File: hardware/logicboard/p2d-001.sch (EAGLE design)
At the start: 54 parts, among them IC1 74LS06N, IC2 4066N, J1 MKR, J2 GPIO, J3 Vcc, J4 RLY, J5 SPI, K1 G5V1, T1 2SC1815, U1 DS18B20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

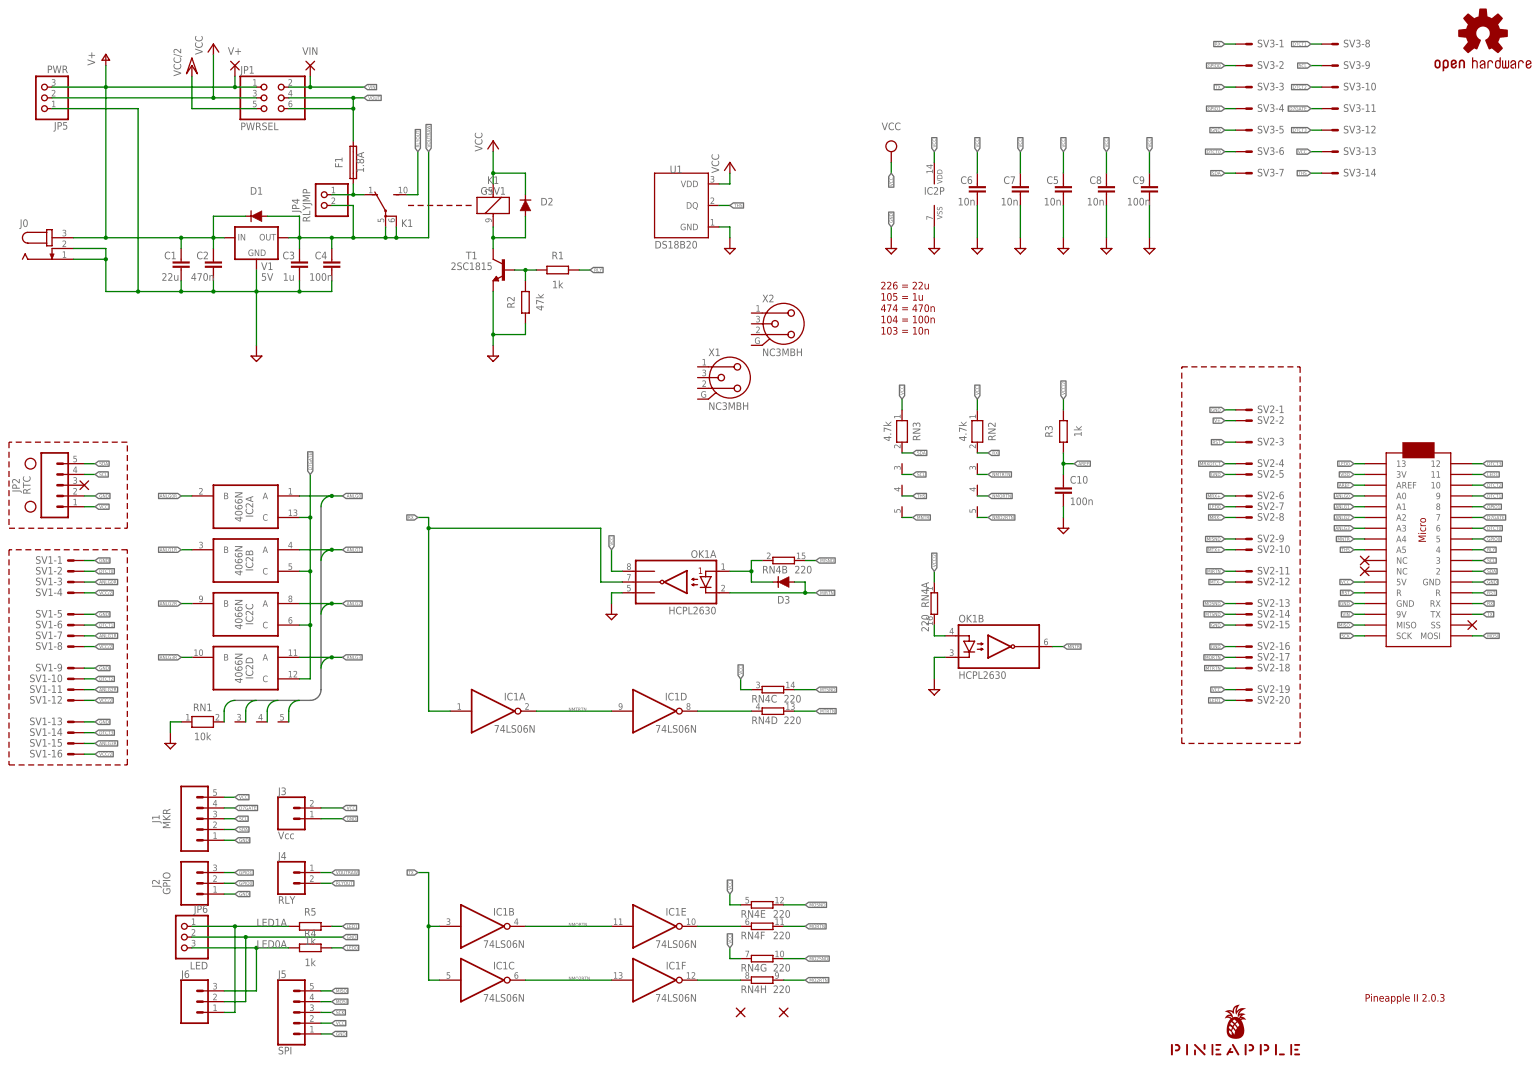
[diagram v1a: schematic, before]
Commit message: Put all parts on board.
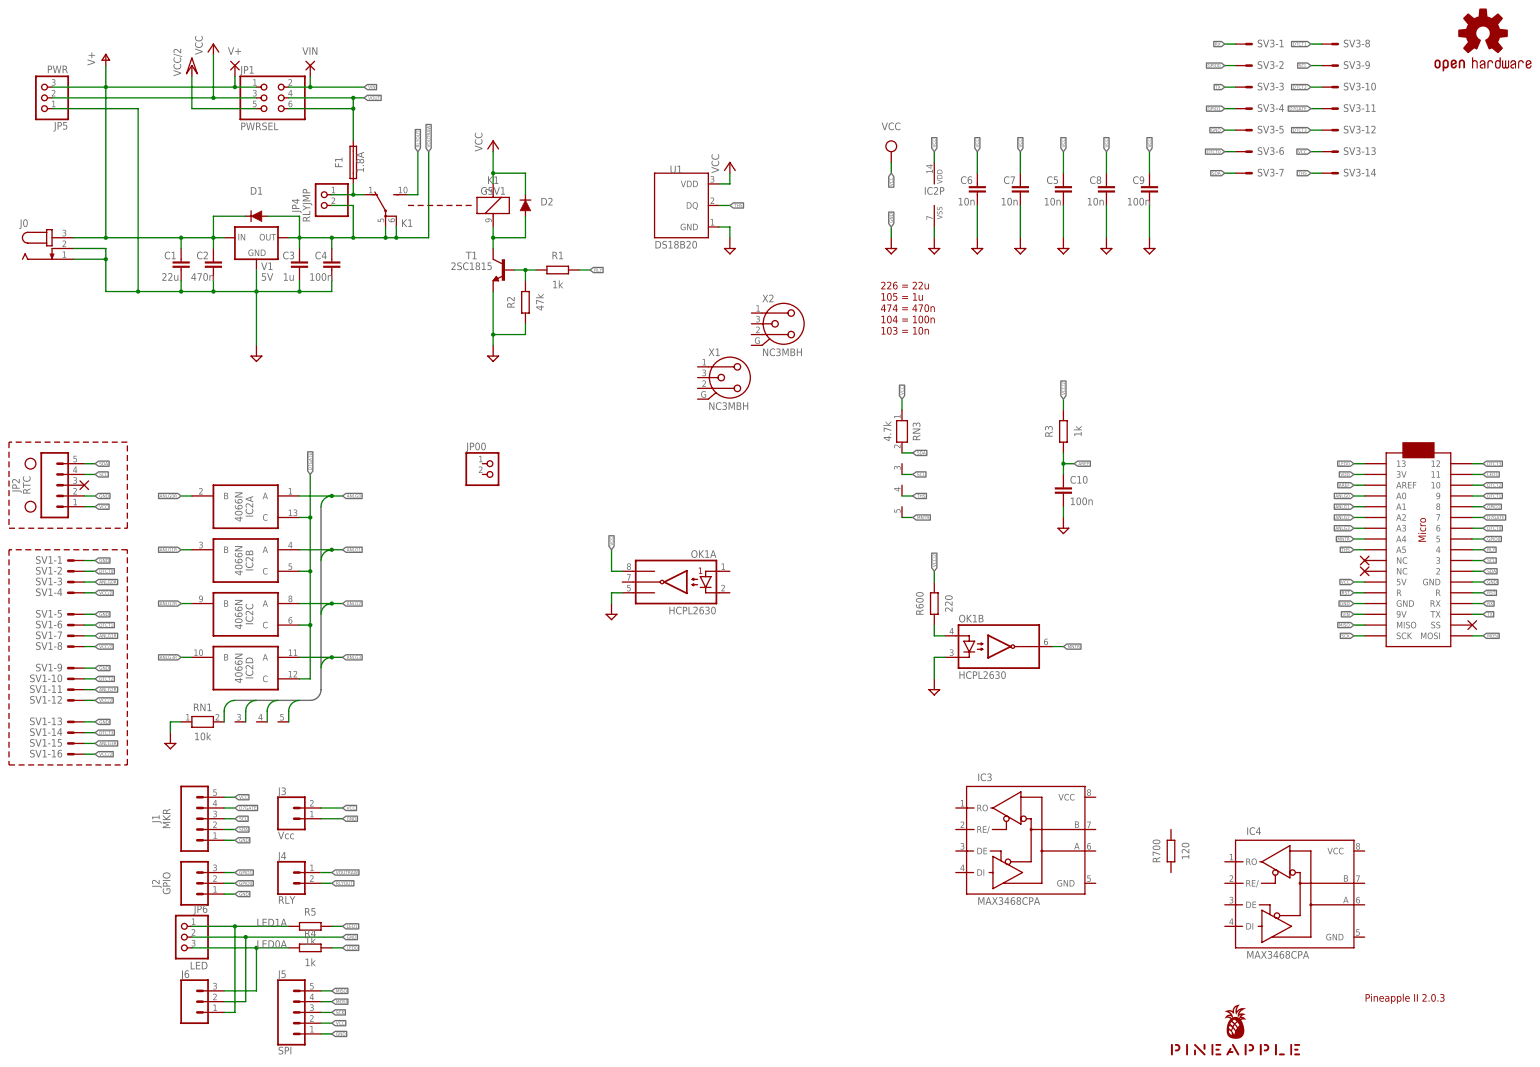
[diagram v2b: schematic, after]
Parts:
- removed D3: DIODE-1N4148, SparkFun-DiscreteSemi:DIODE-1N4148
- removed IC1: 74LS06N, 74xx-us:74LS06N
- removed RN2: 4.7k, resistor-net:RN04
- removed RN4: 220, resistor-dil:8R-N
- removed SV2: (no value), con-ml:ML20LE
- added IC3, IC4: MAX3468CPA, maxim:MAX3468CPA
- added JP00: (no value), pinhead:PINHD-1X2
- added R600: 220, resistor:R-EU_0204/5
- added R700: 120, resistor:R-EU_0204/5
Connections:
- removed net MIDIINSND: D3.C, OK1A.A1, RN4B.1
- removed net MIRTN: D3.A, OK1A.C1, SV2-11.S
- removed net MISND: RN4B.2, SV2-9.S
- removed net MO2RTN: RN4H.2
- removed net MO2RTNRAW: IC1F.O, RN4H.1
- removed net MO2SND: RN4G.2
- removed net MORTN: RN4F.2, SV2-17.S
- removed net MORTNRAW: IC1E.O, RN4F.1
- removed net MOSND: RN4E.2, SV2-13.S
- removed net MRX+: SV2-6.S
- removed net MRX-: SV2-8.S
- removed net MRXDTCT: SV2-4.S
- removed net MTRTN: RN4D.2, SV2-18.S
- removed net MTRTNRAW: IC1D.O, RN4D.1
- removed net MTSND: RN4C.2, SV2-14.S
- removed net MTX+: SV2-10.S
- removed net MTX-: SV2-12.S
- removed net NMO2RTN: IC1C.O, IC1F.I, RN2.5
- removed net NMORTN: IC1B.O, IC1E.I, RN2.4
- removed net NMTRTN: IC1A.O, IC1D.I, RN2.3
- net GND: no longer SV2-1.S, SV2-15.S, SV2-16.S, SV2-5.S
- net LED0: no longer SV2-7.S
- net LED1: no longer SV2-20.S
- net MNTRA: now also R600.1; no longer RN4A.2
- net RST: no longer SV2-3.S
- net RX: no longer IC1A.I, OK1A.VO1, RN2.2
- net TX: no longer IC1B.I, IC1C.I
- net V+: no longer SV2-2.S
- net VCC: no longer RN2.1, RN4C.1, RN4E.1, RN4G.1, SV2-19.S
- net VCC/2: now also R600.2; no longer RN4A.1

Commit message: Design of transceiver.
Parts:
- removed IC4: MAX3468CPA, maxim:MAX3468CPA
- added JP03SELFTERMINATE: (no value), pinhead:PINHD-1X2
- renumbered JP00 to JP00RST
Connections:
- new net DATA+: IC3.A, R700.1, X1.3, X2.3
- new net DATA-: IC3.B, JP03SELFTERMINATE.2, X1.2, X2.2
- new net N$1: JP03SELFTERMINATE.1, R700.2
- net GND: now also IC3.GND, JP00RST.2, OK1A.A1, OK1A.C1, X1.1, X1.G, X2.1, X2.G
- net LED1: now also IC3.DE, IC3.RE/
- net RST: now also JP00RST.1
- net RX: now also IC3.RO
- net TX: now also IC3.DI
- net VCC: now also IC3.VCC
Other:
- moved on the sheet: IC3, R700, X1, X2

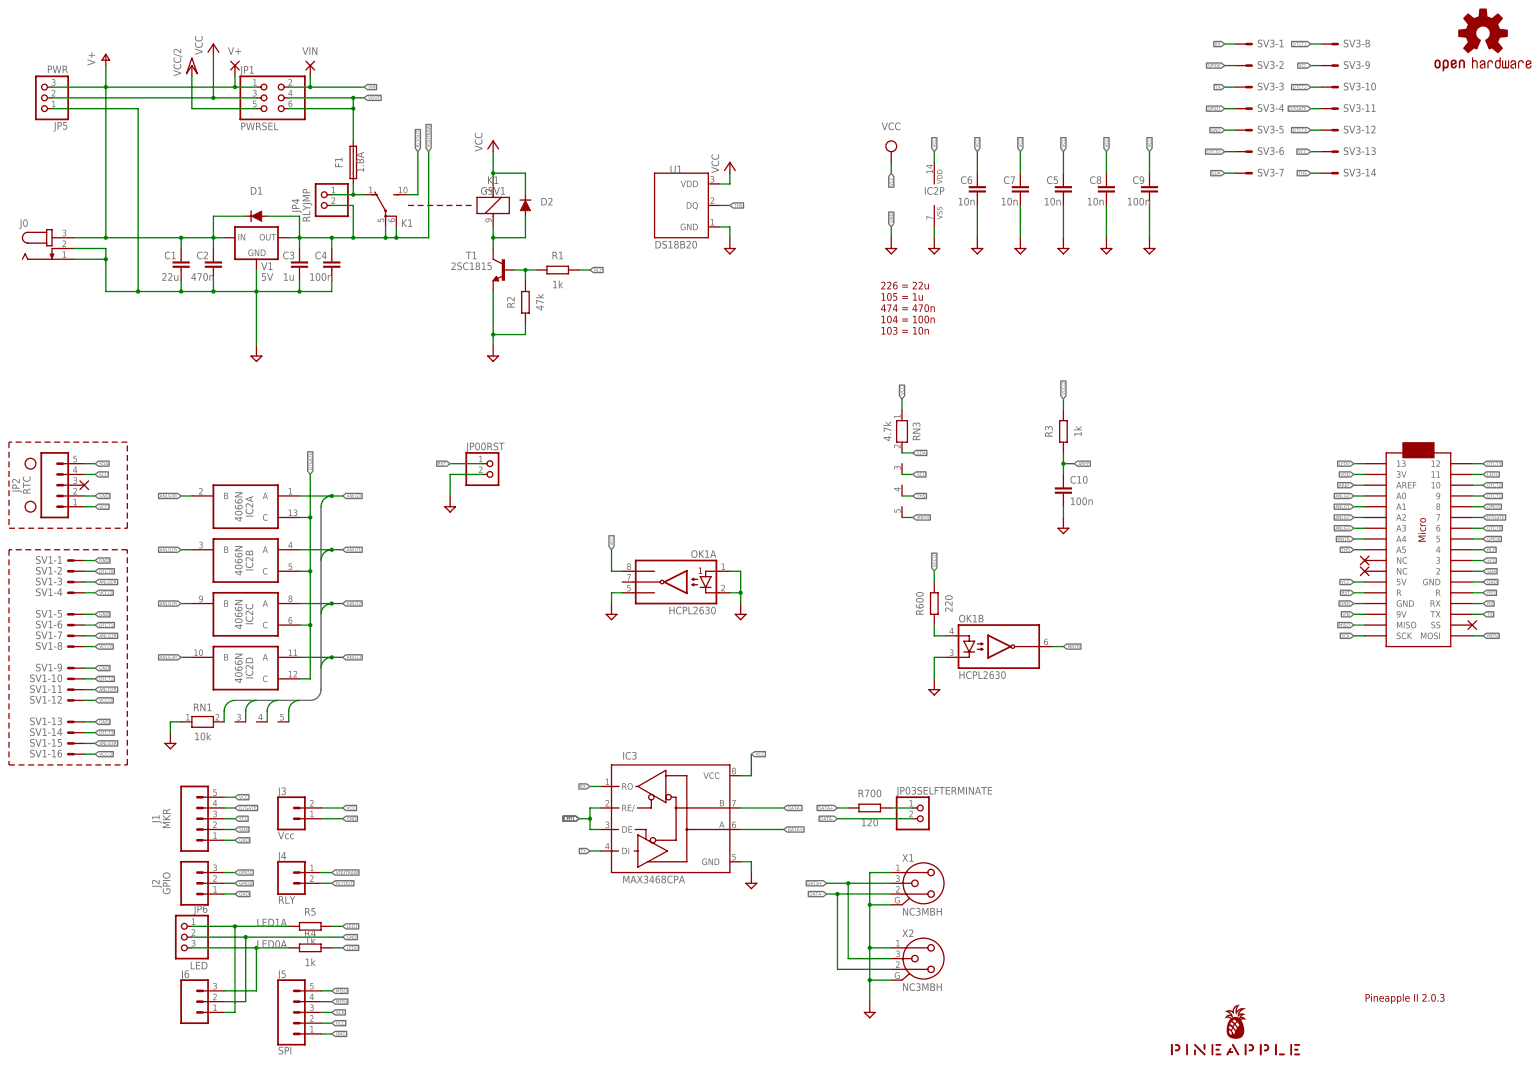
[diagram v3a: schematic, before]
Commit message: Get MIDI back.
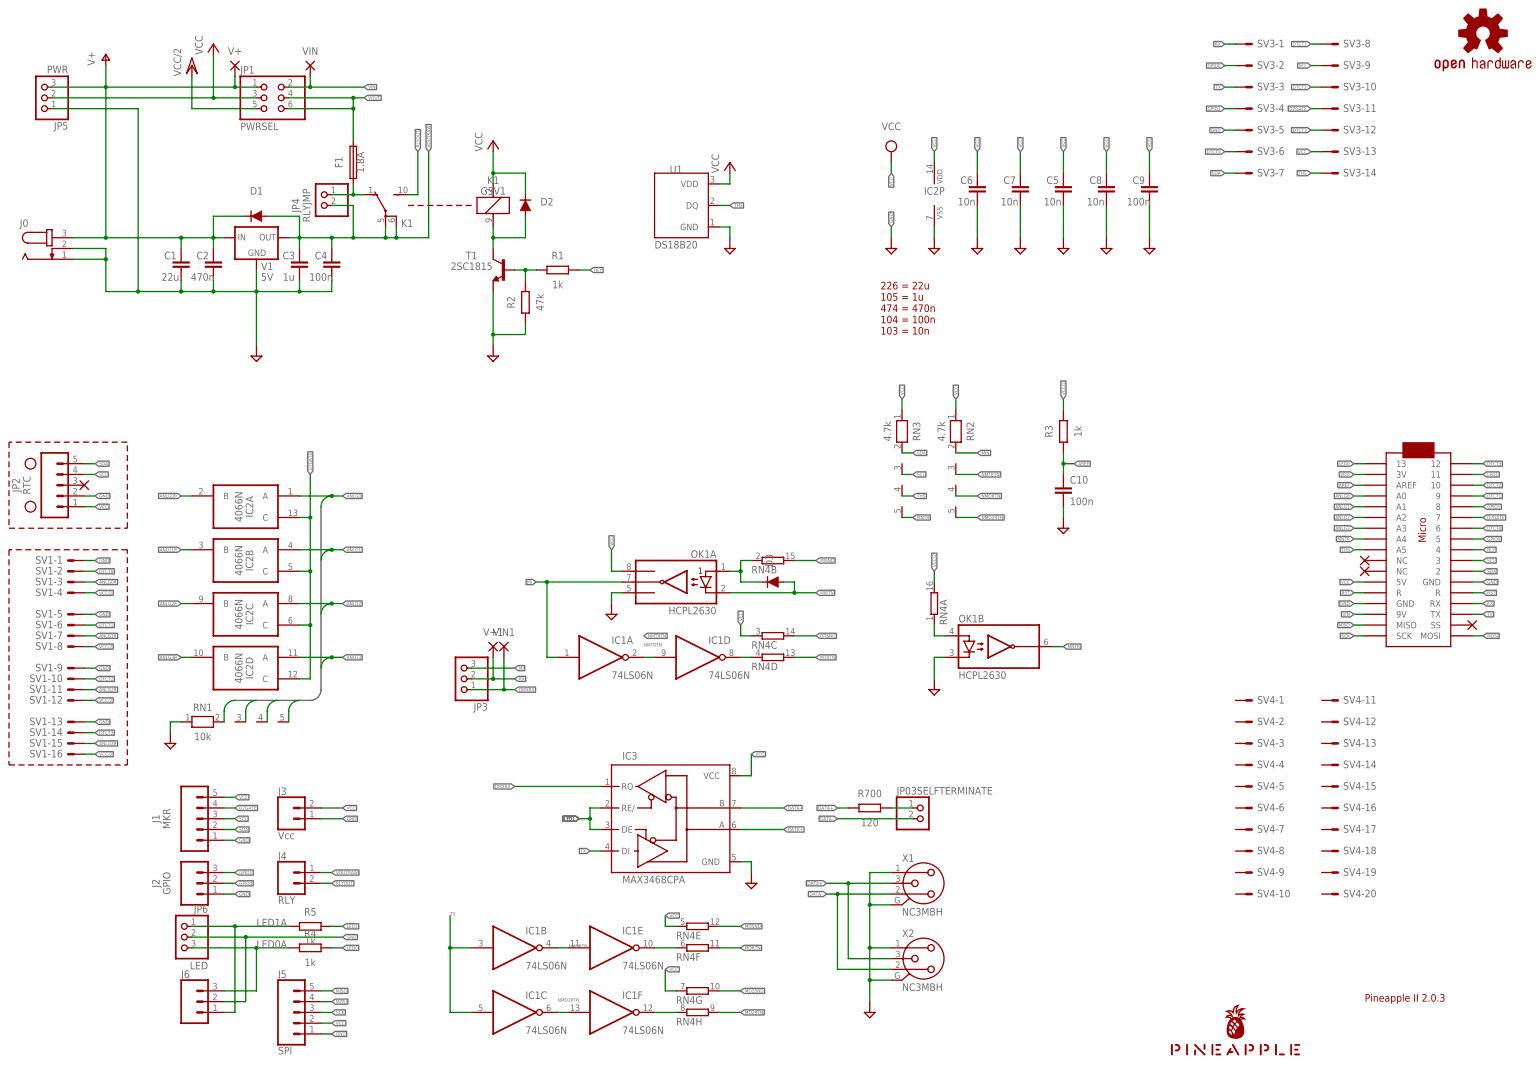
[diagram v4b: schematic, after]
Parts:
- removed JP00RST: (no value), pinhead:PINHD-1X2
- removed R600: 220, resistor:R-EU_0204/5
- added D3: DIODE-1N4148, SparkFun-DiscreteSemi:DIODE-1N4148
- added IC1: 74LS06N, 74xx-us:74LS06N
- added JP3: (no value), pinhead:PINHD-1X3
- added RN2: 4.7k, resistor-net:RN04
- added RN4: (no value), resistor-dil:8R-N
- added SV4: (no value), con-ml:ML20LE
- added V+1, VIN1: (no value), wirepad:SMD2
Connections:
- new net DMXRX: IC3.RO, JP3.1, VIN1.P
- new net MI: IC1A.I, JP3.3, OK1A.VO1
- new net MIN: RN2.2
- new net MIRTN: D3.A, OK1A.C1
- new net MISND: RN4B.2
- new net MO2RTN: RN4H.2
- new net MO2SND: RN4G.2
- new net MORTN: RN4F.2
- new net MOSND: RN4E.2
- new net MTRTN: RN4D.2
- new net MTSND: RN4C.2
- new net N$2: D3.C, OK1A.A1, RN4B.1
- new net N$3: IC1E.O, RN4F.1
- new net N$4: IC1F.O, RN4H.1
- new net N$5: IC1D.O, RN4D.1
- new net NMO2RTN: IC1C.O, IC1F.I, RN2.5
- new net NMORTN: IC1B.O, IC1E.I, RN2.4
- new net NMTRTN: IC1A.O, IC1D.I, RN2.3
- net GND: no longer JP00RST.2, OK1A.A1, OK1A.C1
- net MNTRA: now also RN4A.1; no longer R600.1
- net RST: no longer JP00RST.1
- net RX: now also JP3.2, V+1.P; no longer IC3.RO
- net TX: now also IC1B.I, IC1C.I
- net VCC: now also RN2.1, RN4C.1, RN4E.1, RN4G.1
- net VCC/2: now also RN4A.2; no longer R600.2
